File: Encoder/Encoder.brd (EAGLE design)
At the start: 9 x 12.5 mm, 7 parts, among them IC2 TINY13-20SSU

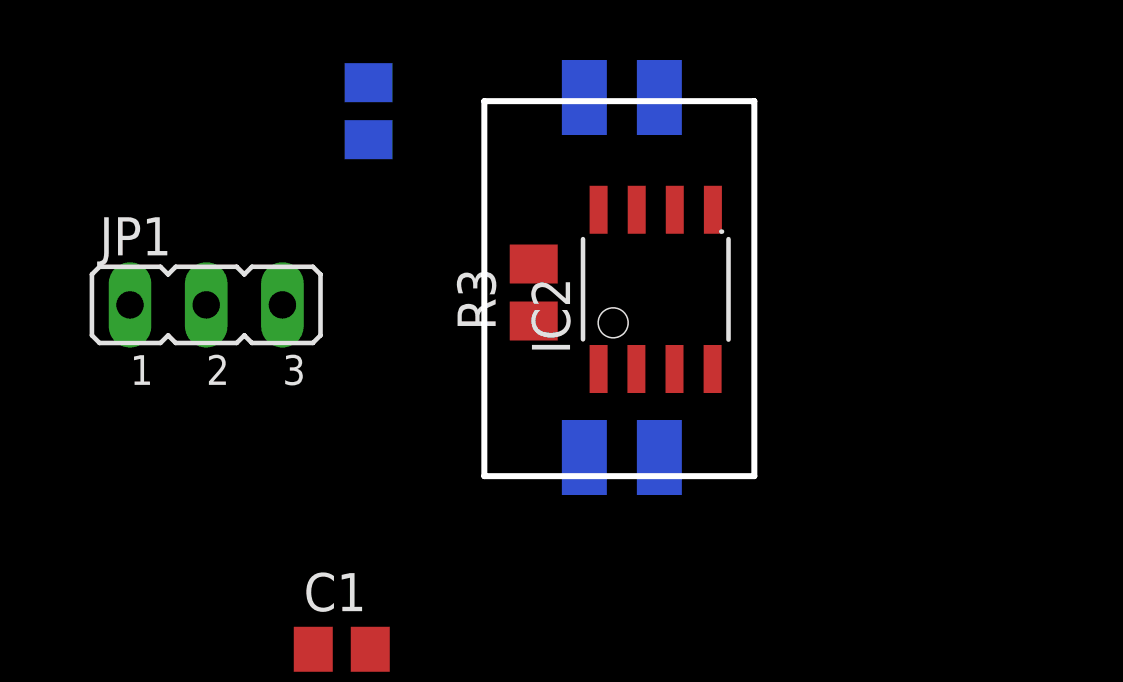
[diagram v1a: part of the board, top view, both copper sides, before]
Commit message: Added connector for programmer. Increased the place for the encoder.
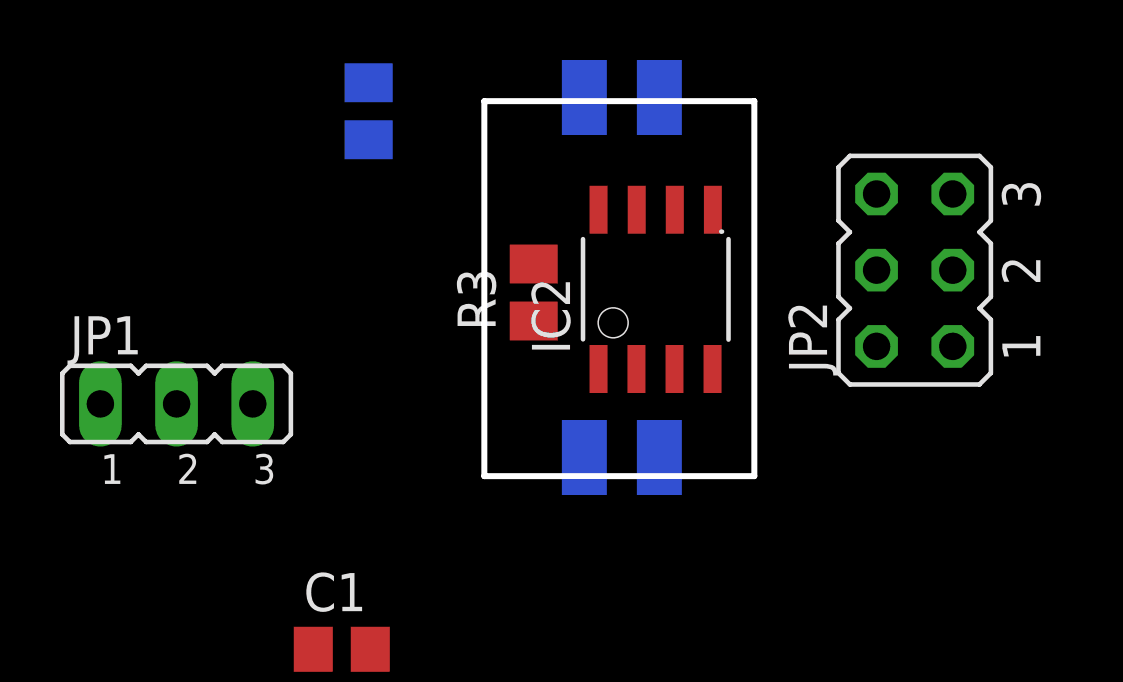
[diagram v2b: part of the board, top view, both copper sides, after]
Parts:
- added JP2: ISP, jumper:JP3Q
- moved JP1 3.45 mm to (23.7, 54.9)
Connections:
- new net N$1: IC2.6, JP2.1
- new net N$3: IC2.7, JP2.3
- net !RES: now also JP2.5
- net +5V: now also JP2.2
- net DATA-IN: now also JP2.4
- net GND: now also JP2.6
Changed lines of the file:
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@@
 <drawing>
 <settings>
-<setting alwaysvectorfont="no"/>
+<setting alwaysvectorfont="yes"/>
 <setting verticaltext="up"/>
 </settings>
@@
 <attribute name="VALUE" x="27.9783" y="44.18880625" size="1.27" layer="27"/>
 </element>
-<element name="JP1" library="jumper" library_urn="urn:adsk.eagle:library:252" package="JP2" package3d_urn="urn:adsk.eagle:package:15452/1" value="" x="24.729278125" y="58.20860625" smashed="yes">
-<attribute name="NAME" x="21.173278125" y="59.85960625" size="1.27" layer="25" ratio="10"/>
-<attribute name="POPULARITY" value="34" x="42.509278125" y="37.88860625" size="1.778" layer="27" display="off"/>
-<attribute name="VALUE" x="21.173278125" y="53.89060625" size="1.27" layer="27" ratio="10"/>
+<element name="JP1" library="jumper" library_urn="urn:adsk.eagle:library:252" package="JP2" package3d_urn="urn:adsk.eagle:package:15452/1" value="" x="23.741759375" y="54.907690625" smashed="yes">
+<attribute name="NAME" x="20.185759375" y="56.558690625" size="1.27" layer="25" ratio="10"/>
+<attribute name="POPULARITY" value="34" x="41.521759375" y="34.587690625" size="1.778" layer="27" display="off"/>
+<attribute name="VALUE" x="20.185759375" y="50.589690625" size="1.27" layer="27" ratio="10"/>
 </element>
 <element name="R1" library="rcl" library_urn="urn:adsk.eagle:library:334" package="M0805" package3d_urn="urn:adsk.eagle:package:23556/2" value="" x="30.141446875" y="64.663434375" smashed="yes" rot="MR270">
@@
 </element>
 <element name="U$1" library="EncoderLib" package="ITR-9608-FOOTPRINT" value="ITR-9608" x="38.584378125" y="59.12145625" smashed="yes" rot="MR0"/>
+<element name="JP2" library="jumper" library_urn="urn:adsk.eagle:library:252" package="JP3Q" package3d_urn="urn:adsk.eagle:package:15460/1" value="ISP" x="48.34530625" y="59.36528125" smashed="yes" rot="R90">
+<attribute name="NAME" x="45.42430625" y="55.93628125" size="1.27" layer="25" ratio="10" rot="R90"/>
+<attribute name="POPULARITY" value="5" x="48.34530625" y="59.36528125" size="1.778" layer="27" rot="R90" display="off"/>
+<attribute name="VALUE" x="54.18730625" y="55.93628125" size="1.27" layer="27" ratio="10" rot="R90"/>
+</element>
 </elements>
 <signals>
@@
 <contactref element="IC2" pad="8"/>
 <contactref element="C1" pad="1"/>
+<contactref element="JP2" pad="2"/>
 <wire x1="35.646875" y1="59.571234375" x2="37.809259375" y2="61.3793" width="0" layer="19" extent="1-1"/>
-<wire x1="27.269278125" y1="58.20860625" x2="35.646875" y2="59.571234375" width="0" layer="19" extent="1-1"/>
-<wire x1="28.2983" y1="46.72880625" x2="27.269278125" y2="58.20860625" width="0" layer="19" extent="1-1"/>
+<wire x1="30.141446875" y1="63.713434375" x2="35.646875" y2="59.571234375" width="0" layer="19" extent="1-16"/>
+<wire x1="26.281759375" y1="54.907690625" x2="30.141446875" y2="63.713434375" width="0" layer="19" extent="16-16"/>
+<wire x1="28.2983" y1="46.72880625" x2="26.281759375" y2="54.907690625" width="0" layer="19" extent="1-1"/>
 <wire x1="36.51" y1="40.64" x2="28.2983" y2="46.72880625" width="0" layer="19" extent="1-1"/>
-<wire x1="30.141446875" y1="63.713434375" x2="36.51" y2="40.64" width="0" layer="19" extent="1-16"/>
+<wire x1="47.07530625" y1="56.82528125" x2="28.2983" y2="46.72880625" width="0" layer="19" extent="1-1"/>
 </signal>
 <signal name="GND">
@@
 <contactref element="U$1" pad="K"/>
 <contactref element="U$1" pad="E"/>
-<wire x1="37.334378125" y1="53.12145625" x2="39.834378125" y2="65.12145625" width="0" layer="19" extent="16-16"/>
-<wire x1="41.609259375" y1="56.0713" x2="37.334378125" y2="53.12145625" width="0" layer="19" extent="1-16"/>
-<wire x1="30.1983" y1="46.72880625" x2="41.609259375" y2="56.0713" width="0" layer="19" extent="1-1"/>
-<wire x1="22.189278125" y1="58.20860625" x2="30.1983" y2="46.72880625" width="0" layer="19" extent="1-1"/>
+<contactref element="JP2" pad="6"/>
+<wire x1="41.609259375" y1="56.0713" x2="39.834378125" y2="65.12145625" width="0" layer="19" extent="1-16"/>
+<wire x1="37.334378125" y1="53.12145625" x2="41.609259375" y2="56.0713" width="0" layer="19" extent="1-16"/>
+<wire x1="30.1983" y1="46.72880625" x2="37.334378125" y2="53.12145625" width="0" layer="19" extent="1-16"/>
+<wire x1="21.201759375" y1="54.907690625" x2="30.1983" y2="46.72880625" width="0" layer="19" extent="1-1"/>
+<wire x1="47.07530625" y1="61.90528125" x2="30.1983" y2="46.72880625" width="0" layer="19" extent="1-1"/>
 </signal>
 <signal name="N$2">
@@
 <contactref element="U$1" pad="C"/>
 <contactref element="IC2" pad="5"/>
+<contactref element="JP2" pad="4"/>
 <wire x1="39.834378125" y1="53.12145625" x2="41.619259375" y2="61.3793" width="0" layer="19" extent="1-16"/>
 <wire x1="34.61" y1="40.64" x2="39.834378125" y2="53.12145625" width="0" layer="19" extent="1-16"/>
+<wire x1="47.07530625" y1="59.36528125" x2="34.61" y2="40.64" width="0" layer="19" extent="1-1"/>
 </signal>
 <signal name="!RES">
 <contactref element="R3" pad="1"/>
 <contactref element="IC2" pad="1"/>
+<contactref element="JP2" pad="5"/>
 <wire x1="37.809259375" y1="56.0713" x2="35.646875" y2="57.671234375" width="0" layer="19" extent="1-1"/>
+<wire x1="49.61530625" y1="61.90528125" x2="35.646875" y2="57.671234375" width="0" layer="19" extent="1-1"/>
 </signal>
 <signal name="DATA-OUT">
 <contactref element="IC2" pad="3"/>
 <contactref element="JP1" pad="2"/>
-<wire x1="24.729278125" y1="58.20860625" x2="40.339259375" y2="56.0713" width="0" layer="19" extent="1-1"/>
+<wire x1="23.741759375" y1="54.907690625" x2="40.339259375" y2="56.0713" width="0" layer="19" extent="1-1"/>
+</signal>
+<signal name="N$1">
+<contactref element="JP2" pad="1"/>
+<contactref element="IC2" pad="6"/>
+<wire x1="49.61530625" y1="56.82528125" x2="40.349259375" y2="61.3793" width="0" layer="19" extent="1-1"/>
+</signal>
+<signal name="N$3">
+<contactref element="JP2" pad="3"/>
+<contactref element="IC2" pad="7"/>
+<wire x1="49.61530625" y1="59.36528125" x2="39.079259375" y2="61.3793" width="0" layer="19" extent="1-1"/>
 </signal>
 </signals>
